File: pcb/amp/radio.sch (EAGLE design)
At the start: 9 parts, among them IC1 LM1117S, U1 TEA5767, X1 22-23-2031, X2 BU-SMA-V

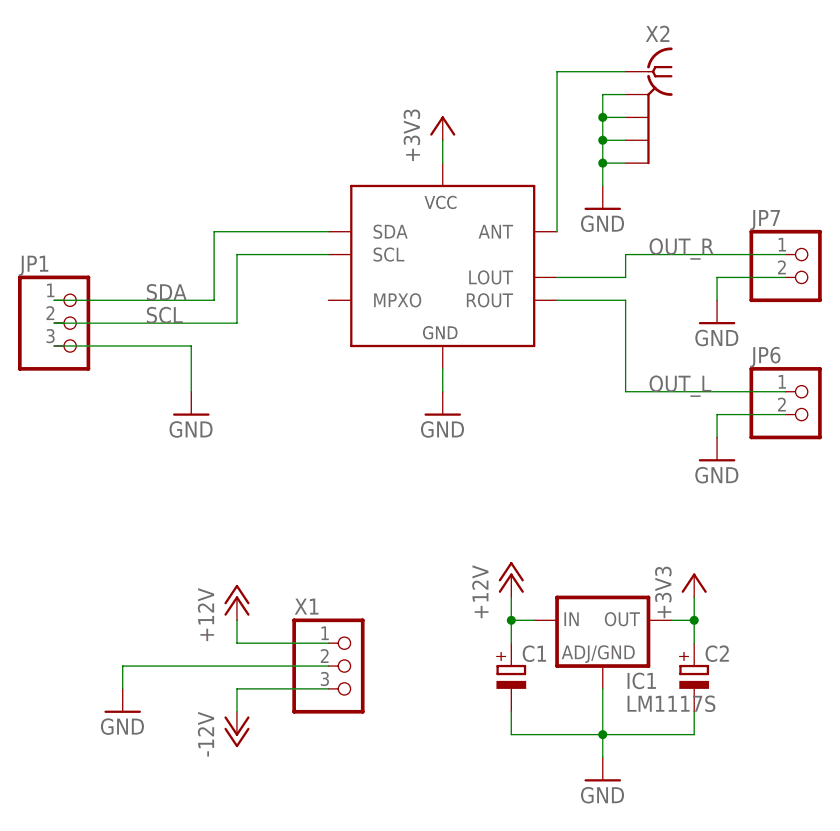
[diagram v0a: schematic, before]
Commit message: 
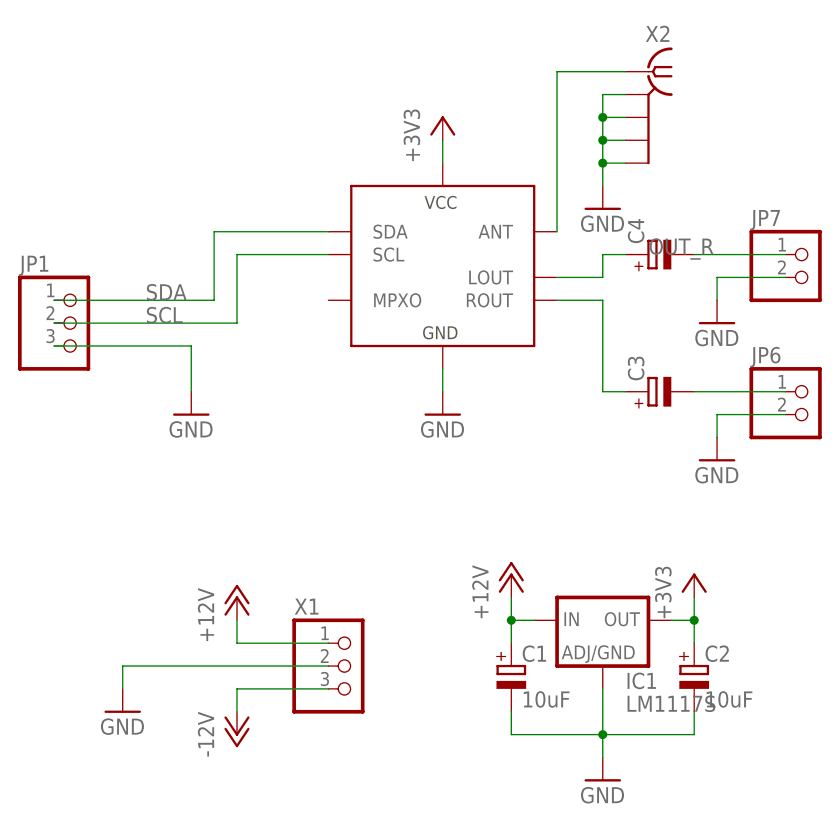
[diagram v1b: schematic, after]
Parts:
- added C3, C4: (no value), amp:CPOL-EUD
- C1, C2: value (none) -> 10uF
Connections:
- removed net OUT_L: JP6.1, U1.ROUT
- new net N$2: C3.+, U1.ROUT
- new net N$3: C3.-, JP6.1
- new net N$4: C4.-, JP7.1
- net OUT_R: now also C4.+; no longer JP7.1
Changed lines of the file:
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@@
 <?xml version="1.0" encoding="utf-8"?>
 <!DOCTYPE eagle SYSTEM "eagle.dtd">
-<eagle version="6.2">
+<eagle version="6.1">
 <drawing>
 <settings>
@@
 <part name="JP1" library="amp" deviceset="PINHD-1X3" device="180"/>
 <part name="GND3" library="amp" deviceset="GND" device=""/>
-<part name="C1" library="amp" deviceset="CPOL-EU" device="SMD"/>
-<part name="C2" library="amp" deviceset="CPOL-EU" device="SMD"/>
+<part name="C1" library="amp" deviceset="CPOL-EU" device="SMD" value="10uF"/>
+<part name="C2" library="amp" deviceset="CPOL-EU" device="SMD" value="10uF"/>
 <part name="X2" library="amp" deviceset="BU-SMA-V" device="" value=""/>
 <part name="GND4" library="amp" deviceset="GND" device=""/>
@@
 <part name="GND6" library="amp" deviceset="GND" device=""/>
 <part name="GND7" library="amp" deviceset="GND" device=""/>
+<part name="C3" library="amp" deviceset="CPOL-EU" device="D"/>
+<part name="C4" library="amp" deviceset="CPOL-EU" device="D"/>
 </parts>
 <sheets>
@@
 <instance part="GND6" gate="1" x="83.82" y="50.8"/>
 <instance part="GND7" gate="1" x="83.82" y="35.56"/>
+<instance part="C3" gate="G$1" x="76.2" y="43.18" rot="R90"/>
+<instance part="C4" gate="G$1" x="76.2" y="58.42" rot="R90"/>
 </instances>
 <busses>
@@
 <net name="OUT_R" class="0">
 <segment>
-<wire x1="73.66" y1="58.42" x2="91.44" y2="58.42" width="0.1524" layer="91"/>
 <label x="76.2" y="58.42" size="1.778" layer="95"/>
-<pinref part="JP7" gate="G$1" pin="1"/>
 <pinref part="U1" gate="G$1" pin="LOUT"/>
-<wire x1="66.04" y1="55.88" x2="73.66" y2="55.88" width="0.1524" layer="91"/>
-<wire x1="73.66" y1="55.88" x2="73.66" y2="58.42" width="0.1524" layer="91"/>
-</segment>
-</net>
-<net name="OUT_L" class="0">
-<segment>
-<wire x1="73.66" y1="43.18" x2="91.44" y2="43.18" width="0.1524" layer="91"/>
-<label x="76.2" y="43.18" size="1.778" layer="95"/>
-<pinref part="JP6" gate="G$1" pin="1"/>
-<pinref part="U1" gate="G$1" pin="ROUT"/>
-<wire x1="66.04" y1="53.34" x2="73.66" y2="53.34" width="0.1524" layer="91"/>
-<wire x1="73.66" y1="53.34" x2="73.66" y2="43.18" width="0.1524" layer="91"/>
+<wire x1="66.04" y1="55.88" x2="71.12" y2="55.88" width="0.1524" layer="91"/>
+<wire x1="71.12" y1="55.88" x2="71.12" y2="58.42" width="0.1524" layer="91"/>
+<pinref part="C4" gate="G$1" pin="+"/>
+<wire x1="71.12" y1="58.42" x2="73.66" y2="58.42" width="0.1524" layer="91"/>
 </segment>
 </net>
@@
 </segment>
 </net>
+<net name="N$2" class="0">
+<segment>
+<pinref part="U1" gate="G$1" pin="ROUT"/>
+<wire x1="66.04" y1="53.34" x2="71.12" y2="53.34" width="0.1524" layer="91"/>
+<pinref part="C3" gate="G$1" pin="+"/>
+<wire x1="71.12" y1="53.34" x2="71.12" y2="43.18" width="0.1524" layer="91"/>
+<wire x1="71.12" y1="43.18" x2="73.66" y2="43.18" width="0.1524" layer="91"/>
+</segment>
+</net>
+<net name="N$3" class="0">
+<segment>
+<pinref part="C3" gate="G$1" pin="-"/>
+<pinref part="JP6" gate="G$1" pin="1"/>
+<wire x1="81.28" y1="43.18" x2="91.44" y2="43.18" width="0.1524" layer="91"/>
+</segment>
+</net>
+<net name="N$4" class="0">
+<segment>
+<pinref part="C4" gate="G$1" pin="-"/>
+<pinref part="JP7" gate="G$1" pin="1"/>
+<wire x1="81.28" y1="58.42" x2="91.44" y2="58.42" width="0.1524" layer="91"/>
+</segment>
+</net>

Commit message: 
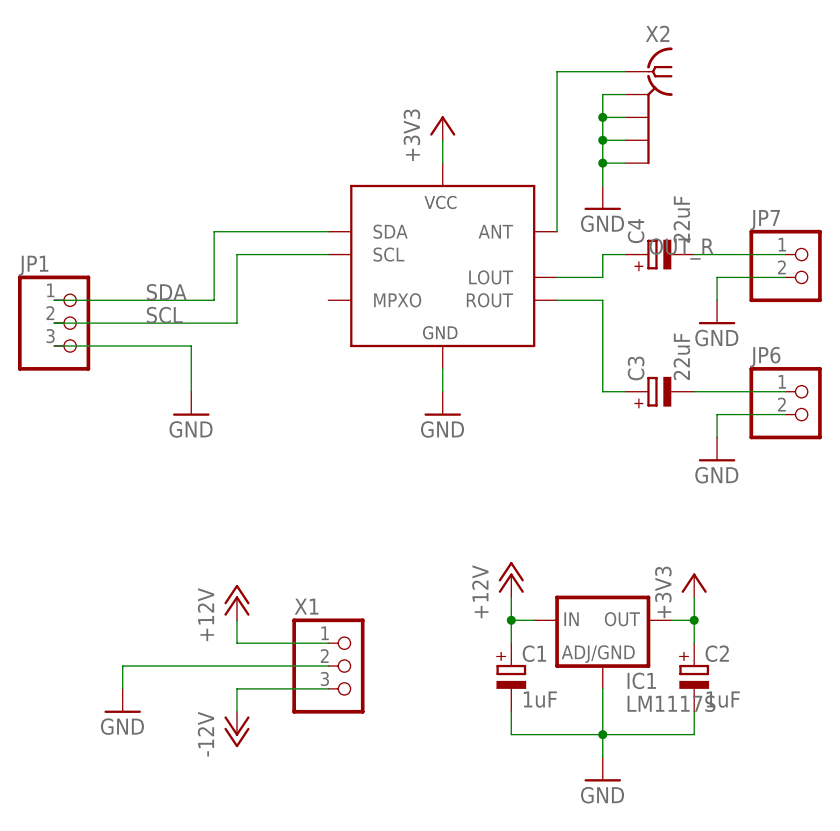
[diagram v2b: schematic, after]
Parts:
- C1, C2: value 10uF -> 1uF
- C3, C4: value (none) -> 22uF
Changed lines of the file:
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@@
 <?xml version="1.0" encoding="utf-8"?>
 <!DOCTYPE eagle SYSTEM "eagle.dtd">
-<eagle version="6.1">
+<eagle version="6.4">
 <drawing>
 <settings>
@@
 <part name="JP1" library="amp" deviceset="PINHD-1X3" device="180"/>
 <part name="GND3" library="amp" deviceset="GND" device=""/>
-<part name="C1" library="amp" deviceset="CPOL-EU" device="SMD" value="10uF"/>
-<part name="C2" library="amp" deviceset="CPOL-EU" device="SMD" value="10uF"/>
+<part name="C1" library="amp" deviceset="CPOL-EU" device="SMD" value="1uF"/>
+<part name="C2" library="amp" deviceset="CPOL-EU" device="SMD" value="1uF"/>
 <part name="X2" library="amp" deviceset="BU-SMA-V" device="" value=""/>
 <part name="GND4" library="amp" deviceset="GND" device=""/>
@@
 <part name="GND6" library="amp" deviceset="GND" device=""/>
 <part name="GND7" library="amp" deviceset="GND" device=""/>
-<part name="C3" library="amp" deviceset="CPOL-EU" device="D"/>
-<part name="C4" library="amp" deviceset="CPOL-EU" device="D"/>
+<part name="C3" library="amp" deviceset="CPOL-EU" device="D" value="22uF"/>
+<part name="C4" library="amp" deviceset="CPOL-EU" device="D" value="22uF"/>
 </parts>
 <sheets>
